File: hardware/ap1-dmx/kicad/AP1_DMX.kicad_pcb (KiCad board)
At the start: 2 copper layers, 88 x 56 mm, 33 parts, among them J1 ENTRADA 12-24V, J2 DMX, J7 PROGRAMADOR, U1 M24C02-WMN6TP, U2 LMR16006XDDC, U3 SP3485EN

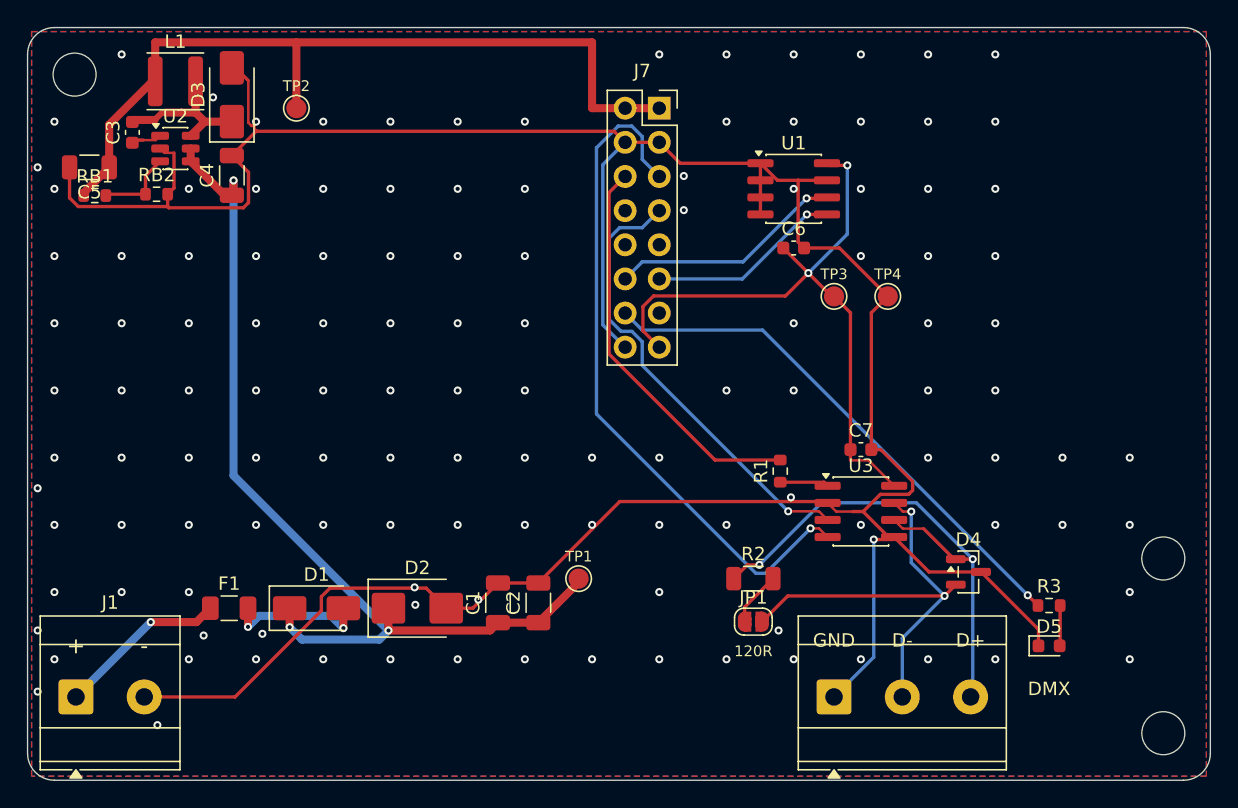
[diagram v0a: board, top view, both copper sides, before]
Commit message: AP CONNECT: sin borneras en todas las placas, placa nueva AP PRO AI4 y guía de fabricantes
- Borneras de tornillo reemplazadas por conectores con cable y código LCSC verificado:
  XT60 (C98732), JST VH 2/3/4 (C160315/6/7), JST XH 2/3/4 (C158012, C144394/5), Qwiic
  en BASE, IND, PIX, DMX, PLANTILLA, AP INPUT, AP OUTPUT y DIST 4; zonas de potencia rehechas
- XT60 de la DIST 4 con la polaridad marcada en la huella (pata 1 = -, pata 2 = +)
- TCA9554PWR ya con código (C477924)
- ap1-ai4: 4 entradas 0-10 V / 4-20 mA con ADS1115 (C37593), +24 V para sensores de lazo
- Programa 1.7: lectura AI4, umbrales con acciones, Home Assistant, tarjeta en la app
- FABRICANTES.md: JLCPCB, PCBWay, Seeed, NextPCB, México; impresión 3D y tornillería
- Pedido JLCPCB con 10 placas (AP-0.2 retirada); ERC/DRC/DFM 0 en todas

Co-Authored-By: Claude Opus 5.5 <noreply@anthropic.com>
Claude-Session: https://claude.ai/code/session_01WVk3oGwfQfGTmAT2PMp8oW
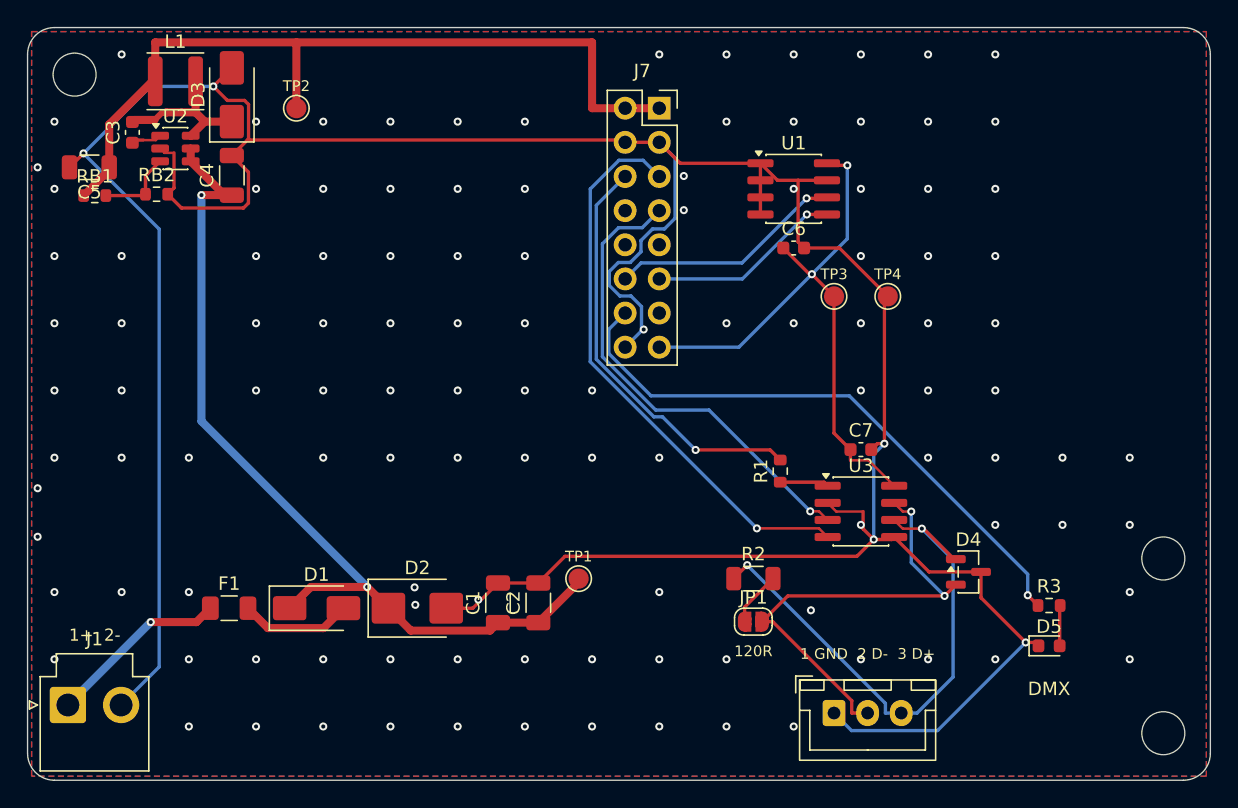
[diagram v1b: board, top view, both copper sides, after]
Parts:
- J1: footprint TerminalBlock_Phoenix:TerminalBlock_Phoenix_MKDS-3-2-5.08_1x02_P5.08mm_Horizontal -> Connector_JST:JST_VH_B2P-VH_1x02_P3.96mm_Vertical
- J2: footprint TerminalBlock_Phoenix:TerminalBlock_Phoenix_MKDS-3-3-5.08_1x03_P5.08mm_Horizontal -> Connector_JST:JST_XH_B3B-XH-A_1x03_P2.50mm_Vertical
- moved J2 1.20 mm to (160.0, 151.0)
- moved J1 0.85 mm to (103.0, 150.4)
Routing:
- net /GND: track 226.1 -> 257.3 mm, vias 128 -> 122
- net /PWM1: track 51.5 -> 42.4 mm
- net /VIN: track 71.5 -> 66.8 mm, vias 3 -> 2
- net /AUX: track 39.7 -> 44.1 mm
- net /3V3: track 49.7 -> 46.4 mm
- net /DMXB: track 33.2 -> 35.6 mm
- net /VF: track 10.7 -> 8.33 mm, vias 2 -> 0
- net /PWM2: track 29.7 -> 31.3 mm, vias 0 -> 1
- net /DMXA: track 39.2 -> 40.6 mm
- net /PWM3: track 34.1 -> 35.4 mm
- net /VIN_RAW: track 12.7 -> 13.6 mm
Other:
- board text added: "1+ 2-"
- board text removed: "+"
- board text removed: "-"
- board text removed: "D+"
- board text removed: "D-"
- board text removed: "GND"
